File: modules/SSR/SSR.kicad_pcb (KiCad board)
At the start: 2 copper layers, 53.8 x 39.2 mm, 36 parts, among them J1 Conn_01x08_Pin, J2 Conn_01x16_Socket, J3 Conn_01x01_Pin, J4 Conn_01x09_Pin

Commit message: production output for SSR module
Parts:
- R1, R10, R11, R12, R13, R14, R15, R16, R2, R3, R4, R5, R6, R7, R8, R9: value R -> 330
- U1, U10, U11, U12, U13, U14, U15, U16, U2, U3, U4, U5, U6, U7, U8, U9: value ~ -> GAQY210S
- moved J2 54.3 mm to (137.1, 153.5), turned to 0 degrees
- moved J3 52.9 mm to (132.5, 172.4)
- moved R10 4.22 mm to (88.5, 188.1)
- moved R11 4.22 mm to (95.1, 188.1)
- moved R12 4.22 mm to (101.2, 188.1)
- moved R13 4.22 mm to (107.6, 188.1)
- moved R14 4.22 mm to (113.8, 188.1)
- moved R15 4.22 mm to (120.3, 188.1)
- moved R16 4.22 mm to (126.6, 188.1)
- moved R9 4.22 mm to (82.4, 188.1)
- moved U10 4.22 mm to (88.8, 183.4)
- moved U11 4.22 mm to (95.1, 183.4)
- moved U12 4.22 mm to (101.2, 183.4)
- moved U13 4.22 mm to (107.6, 183.4)
- moved U14 4.22 mm to (113.8, 183.4)
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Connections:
- J2 pad 1: /SSR/AC1 -> /AC7
- J2 pad 2: /SSR1/AC1 -> /AC6
- J2 pad 3: /SSR2/AC1 -> /AC5
- J2 pad 4: /SSR3/AC1 -> /AC4
- J2 pad 5: /SSR4/AC1 -> /AC3
- J2 pad 6: /SSR5/AC1 -> /AC2
- J2 pad 7: /SSR6/AC1 -> /AC1
- J2 pad 8: /SSR7/AC1 -> /AC0
- U1 pad 3: /SSR/AC1 -> /AC0
- U2 pad 3: /SSR1/AC1 -> /AC1
- U3 pad 3: /SSR2/AC1 -> /AC2
- U4 pad 3: /SSR3/AC1 -> /AC3
- U5 pad 3: /SSR4/AC1 -> /AC4
- U6 pad 3: /SSR5/AC1 -> /AC5
- U7 pad 3: /SSR6/AC1 -> /AC6
- U8 pad 3: /SSR7/AC1 -> /AC7
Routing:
- net /AC0: track 0.00 -> 59.0 mm
- net /AC1: track 0.00 -> 52.3 mm
- net /AC2: track 0.00 -> 46.2 mm
- net /AC3: track 0.00 -> 40.7 mm
- net /AC4: track 0.00 -> 36.1 mm
- net /AC5: track 0.00 -> 32.3 mm
- net /SSR8/AC1: track 24.7 -> 56.1 mm
- net /SSR10/AC1: track 17.1 -> 45.0 mm
- net /SSR9/AC1: track 22.2 -> 49.7 mm
- net /AC6: track 0.00 -> 27.1 mm
- net /SSR11/AC1: track 13.5 -> 39.1 mm
- net /SSR7/AC1: track 24.6 -> 0.00 mm
- net /SSR12/AC1: track 9.69 -> 33.7 mm
- net /AC7: track 0.00 -> 22.7 mm
- net /SSR13/AC1: track 7.64 -> 28.9 mm
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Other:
- board size 53.8 x 39.2 mm -> 62.8 x 43.9 mm
- board text added: "220V AC"

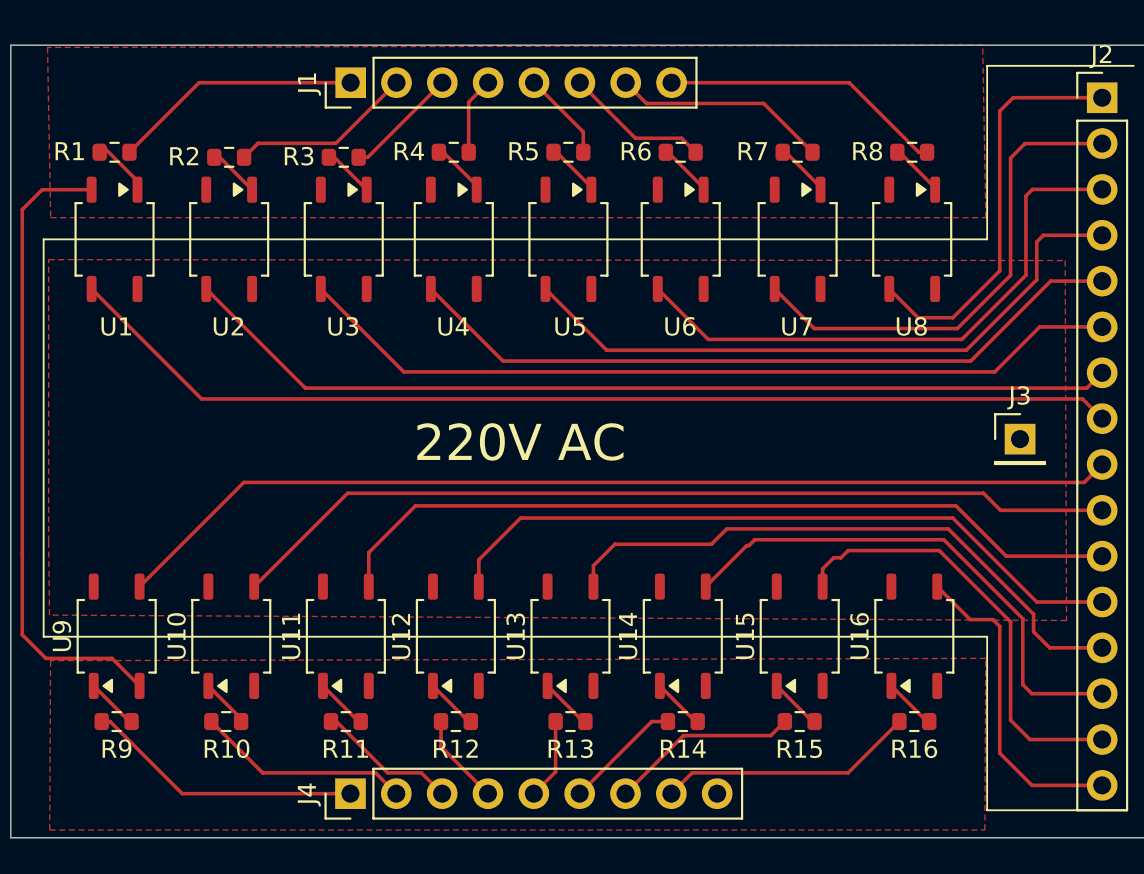
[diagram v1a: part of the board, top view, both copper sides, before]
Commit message: added footprints for modules
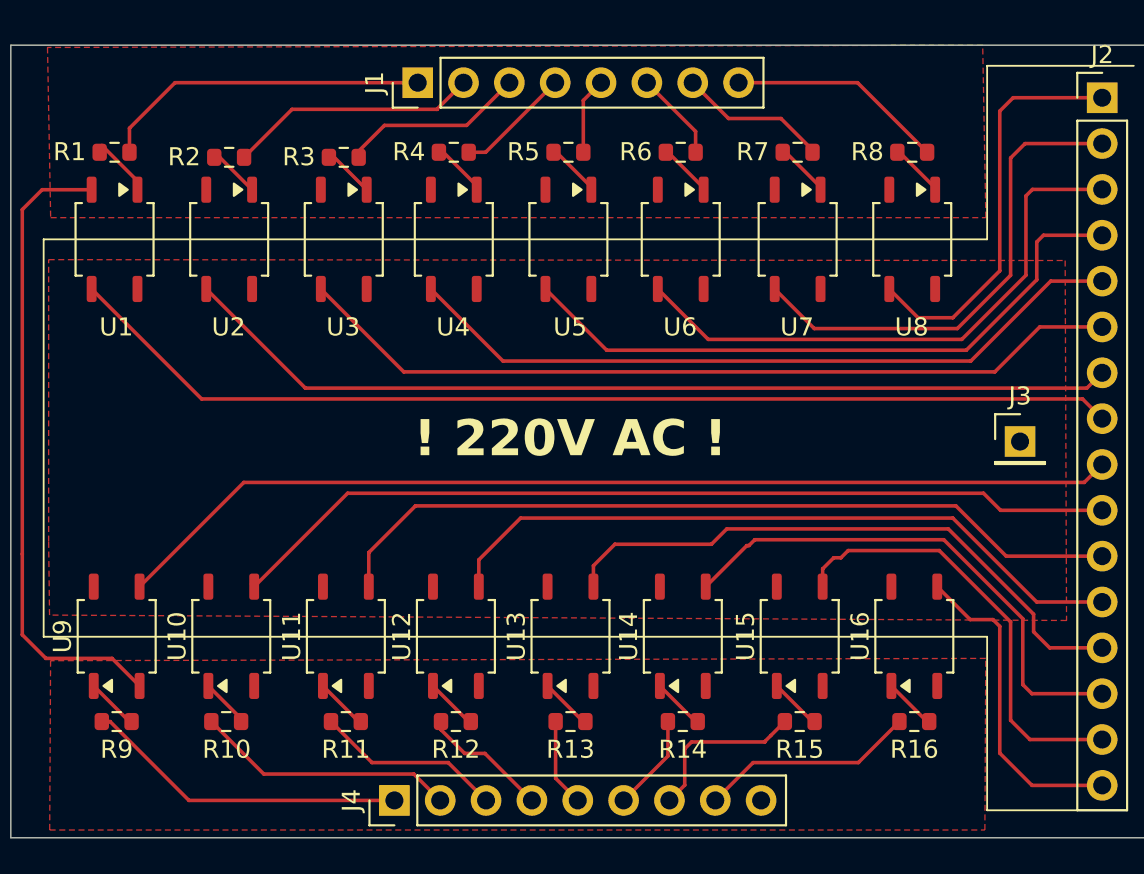
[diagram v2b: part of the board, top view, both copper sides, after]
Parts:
- moved J1 3.71 mm to (99.1, 152.7)
- moved J4 2.46 mm to (97.8, 192.5)
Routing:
- net /SSR/Ctrl: track 13.9 -> 18.3 mm
- net /SSR2/Ctrl: track 6.35 -> 10.3 mm
- net /SSR1/Ctrl: track 10.2 -> 13.9 mm
- net /SSR7/Ctrl: track 15.8 -> 12.0 mm
- net /SSR6/Ctrl: track 11.9 -> 8.31 mm
- net /SSR5/Ctrl: track 8.01 -> 4.97 mm
- net /SSR10/Ctrl: track 7.81 -> 10.7 mm
- net /SSR9/Ctrl: track 11.9 -> 14.5 mm
- net /SSR8/Ctrl: track 15.4 -> 18.0 mm
- net /SSR15/Ctrl: track 14.3 -> 12.0 mm
- net /SSR3/Ctrl: track 4.30 -> 6.39 mm
- net /SSR11/Ctrl: track 5.07 -> 7.11 mm
- net /SSR13/Ctrl: track 6.54 -> 5.39 mm
- net /SSR14/Ctrl: track 10.5 -> 9.40 mm
- net /SSR4/Ctrl: track 4.99 -> 4.26 mm
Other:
- board text added: "! 220V AC !"
- board text removed: "220V AC"

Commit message: routing
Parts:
- removed J4: Conn_01x09_Pin, Connector_PinHeader_2.54mm:PinHeader_1x09_P2.54mm_Vertical
- J1: value Conn_01x08_Pin -> Conn_01x17_Pin; footprint Connector_PinHeader_2.54mm:PinHeader_1x08_P2.54mm_Vertical -> Connector_PinHeader_2.54mm:PinHeader_1x17_P2.54mm_Vertical
- moved J2 89.1 mm to (49.9, 134.8), turned to 90 degrees
- moved J3 71.4 mm to (69.0, 140.0), turned to 90 degrees
- moved U8 66.8 mm to (61.2, 147.5), turned to 90 degrees
- moved R8 65.4 mm to (61.2, 152.2), turned to 0 degrees
- moved U7 65.2 mm to (56.5, 147.5), turned to 90 degrees
- moved R7 63.9 mm to (56.5, 152.2), turned to 0 degrees
- moved U6 63.6 mm to (51.7, 147.5), turned to 90 degrees
- moved R6 62.2 mm to (51.7, 152.2), turned to 0 degrees
- moved U5 62.2 mm to (46.8, 147.5), turned to 90 degrees
- moved R5 60.8 mm to (46.8, 152.2), turned to 0 degrees
- moved U4 60.7 mm to (42.1, 147.5), turned to 90 degrees
- moved U3 59.4 mm to (37.3, 147.5), turned to 90 degrees
- moved R4 59.2 mm to (42.1, 152.2), turned to 0 degrees
- moved R3 58.0 mm to (37.3, 152.2), turned to 0 degrees
- moved U2 57.9 mm to (32.5, 147.4), turned to 90 degrees
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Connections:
- J1 pad 1: /SSR/Ctrl -> GND
- J1 pad 2: /SSR1/Ctrl -> /SSR15/Ctrl
- J1 pad 3: /SSR2/Ctrl -> /SSR14/Ctrl
- J1 pad 4: /SSR3/Ctrl -> /SSR13/Ctrl
- J1 pad 5: /SSR4/Ctrl -> /SSR12/Ctrl
- J1 pad 6: /SSR5/Ctrl -> /SSR11/Ctrl
- J1 pad 7: /SSR6/Ctrl -> /SSR10/Ctrl
- J1 pad 8: /SSR7/Ctrl -> /SSR9/Ctrl
- J2 pad 1: /AC7 -> /AC0
- J2 pad 2: /AC6 -> /AC1
- J2 pad 3: /AC5 -> /AC2
- J2 pad 4: /AC4 -> /AC3
- J2 pad 5: /AC3 -> /AC4
- J2 pad 6: /AC2 -> /AC5
- J2 pad 7: /AC1 -> /AC6
- J2 pad 8: /AC0 -> /AC7
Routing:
- net /SSR8/AC1: track 56.1 -> 11.8 mm
- net /SSR9/AC1: track 49.7 -> 10.2 mm
- net GND: track 35.5 -> 0.00 mm
- net /SSR10/AC1: track 45.0 -> 10.7 mm
- net /AC0: track 59.0 -> 27.4 mm
- net /SSR11/AC1: track 39.1 -> 11.6 mm
- net /AC1: track 52.3 -> 25.3 mm
- net /AC2: track 46.2 -> 22.8 mm
- net /SSR12/AC1: track 33.7 -> 12.6 mm
- net /AC3: track 40.7 -> 21.0 mm
- net /AC4: track 36.1 -> 17.8 mm
- net /AC5: track 32.3 -> 15.3 mm
- net /AC6: track 27.1 -> 13.0 mm
- net /SSR13/AC1: track 28.9 -> 15.2 mm
- net /SSR3/Ctrl: track 6.39 -> 19.3 mm
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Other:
- board outline removed
